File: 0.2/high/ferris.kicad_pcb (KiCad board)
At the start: 2 copper layers, 219.1 x 95.2 mm, 109 parts, among them J1 TYPE-C-31-M-12, K0_0 KEYSW, K0_1 KEYSW, K0_2 KEYSW, K0_3 KEYSW, K0_4 KEYSW, K0_5 KEYSW, K0_6 KEYSW, K0_7 KEYSW, K0_8 KEYSW, K0_9 KEYSW, K1_0 KEYSW, K1_1 KEYSW, K1_2 KEYSW, K1_3 KEYSW, K1_4 KEYSW, K1_5 KEYSW, K1_6 KEYSW, K1_7 KEYSW, K1_8 KEYSW, K1_9 KEYSW, K2_0 KEYSW, K2_1 KEYSW, K2_2 KEYSW, K2_3 KEYSW, K2_4 KEYSW, K2_5 KEYSW, K2_6 KEYSW, K2_7 KEYSW, K2_8 KEYSW, K2_9 KEYSW, K3_3 KEYSW, K3_4 KEYSW, K3_5 KEYSW, K3_6 KEYSW, Q1 PDTC123JT,215, SW1 B3U-1000P, U1 STM32F072CBT6, U2 MCP23017-E/SO, U3 MCP1700T-3302E/TT, U4 SRV05-4

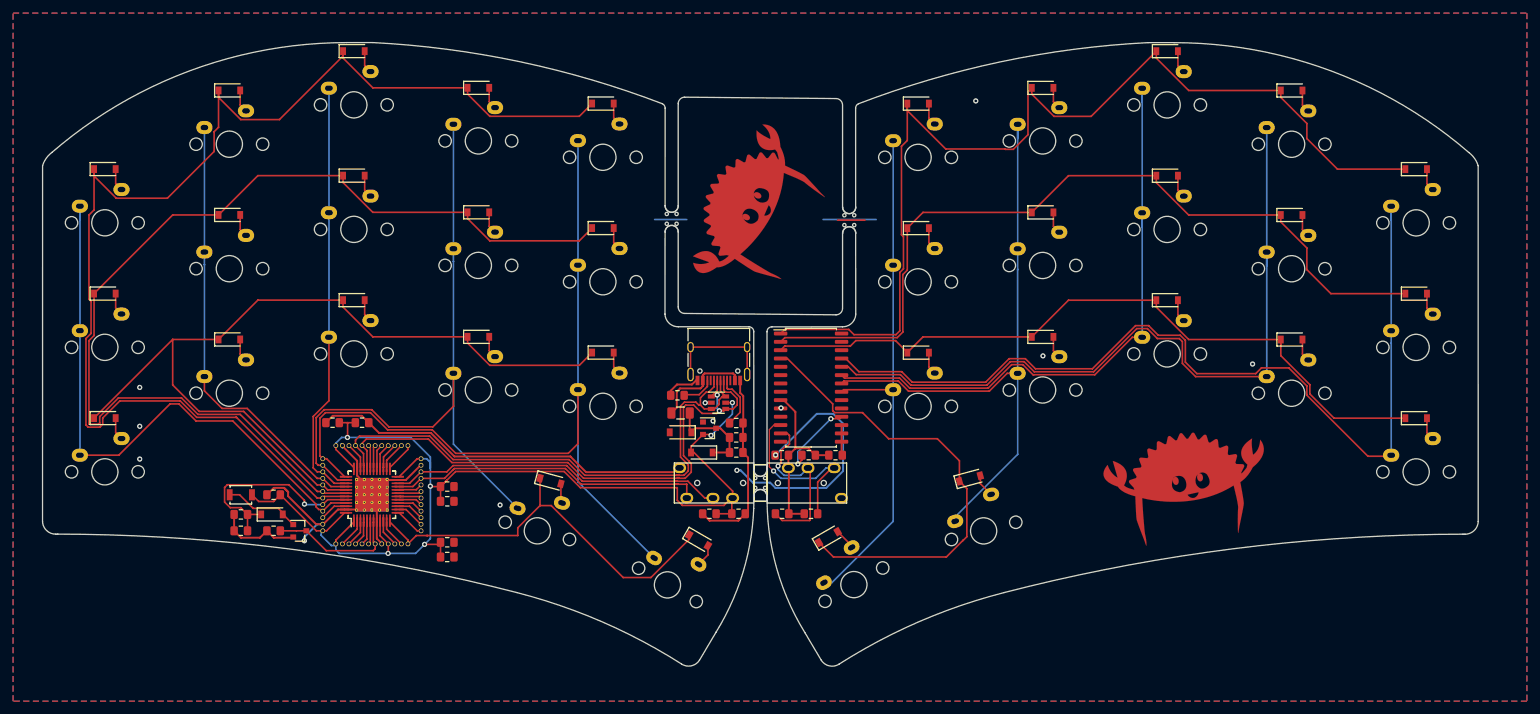
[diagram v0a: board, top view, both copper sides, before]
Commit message: Fix DRC violations down to 163
Mainly hole clearances, would need to fix the 5mm breakaway tab and perhaps solder mask clearances
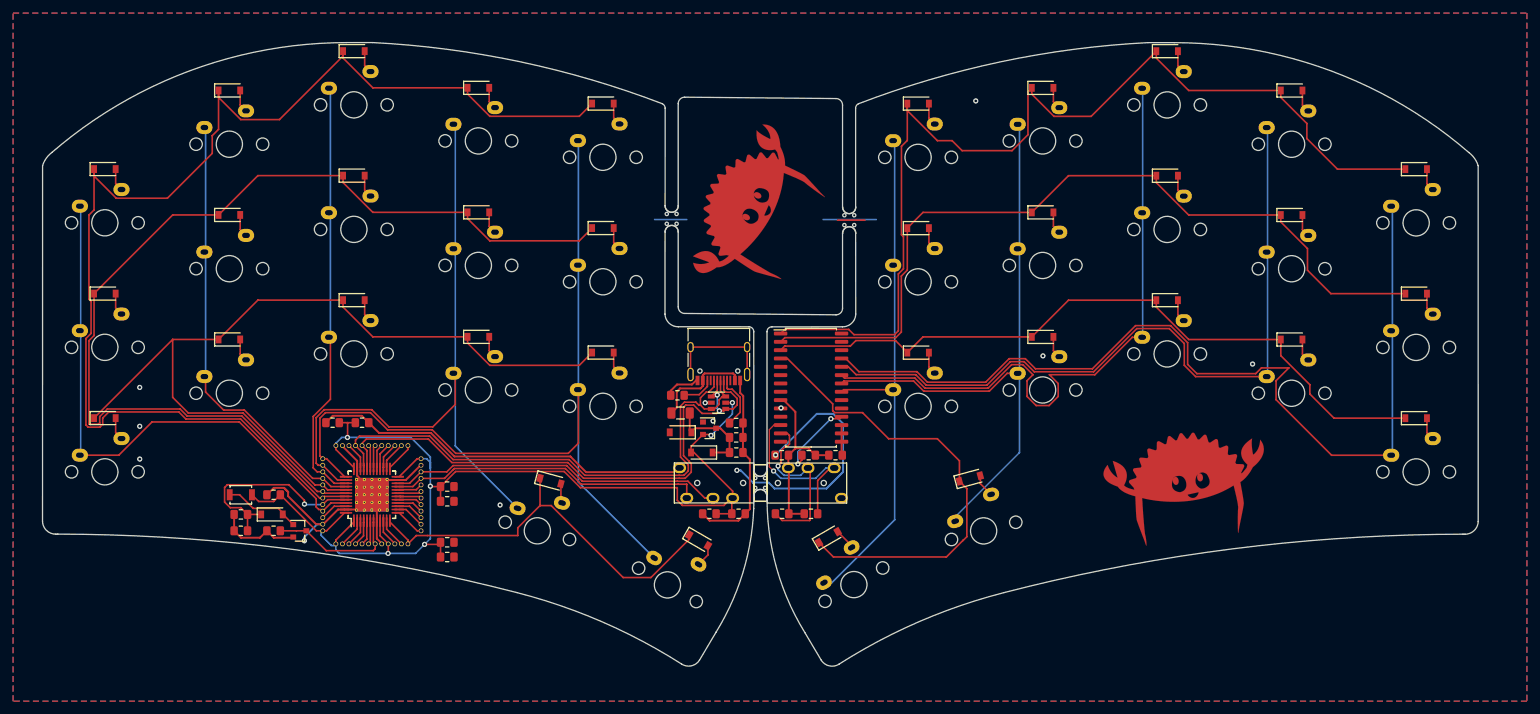
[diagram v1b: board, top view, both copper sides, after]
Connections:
- J1 pad A8: Net-(J1-PadA8) -> unconnected-(J1-SBU1-PadA8)
- J1 pad B8: Net-(J1-PadB8) -> unconnected-(J1-SBU2-PadB8)
- J1 pad S1: Net-(J1-PadS1) -> unconnected-(J1-SHIELD-PadS1)
- U1 pad 10: Net-(U1-Pad10) -> unconnected-(U1-PA0-Pad10)
- U1 pad 11: Net-(U1-Pad11) -> unconnected-(U1-PA1-Pad11)
- U1 pad 13: Net-(U1-Pad13) -> unconnected-(U1-PA3-Pad13)
- U1 pad 14: Net-(U1-Pad14) -> unconnected-(U1-PA4-Pad14)
- U1 pad 15: Net-(U1-Pad15) -> unconnected-(U1-PA5-Pad15)
- U1 pad 16: Net-(U1-Pad16) -> unconnected-(U1-PA6-Pad16)
- U1 pad 17: Net-(U1-Pad17) -> unconnected-(U1-PA7-Pad17)
- U1 pad 18: Net-(U1-Pad18) -> unconnected-(U1-PB0-Pad18)
- U1 pad 19: Net-(U1-Pad19) -> unconnected-(U1-PB1-Pad19)
- U1 pad 2: Net-(U1-Pad2) -> unconnected-(U1-PC13-Pad2)
- U1 pad 20: Net-(U1-Pad20) -> unconnected-(U1-PB2-Pad20)
- U1 pad 25: Net-(U1-Pad25) -> unconnected-(U1-PB12-Pad25)
- U1 pad 26: Net-(U1-Pad26) -> unconnected-(U1-PB13-Pad26)
- U1 pad 27: Net-(U1-Pad27) -> unconnected-(U1-PB14-Pad27)
- U1 pad 28: Net-(U1-Pad28) -> unconnected-(U1-PB15-Pad28)
- U1 pad 29: Net-(U1-Pad29) -> unconnected-(U1-PA8-Pad29)
- U1 pad 3: Net-(U1-Pad3) -> unconnected-(U1-PC14-Pad3)
- U1 pad 30: Net-(U1-Pad30) -> unconnected-(U1-PA9-Pad30)
- U1 pad 31: Net-(U1-Pad31) -> unconnected-(U1-PA10-Pad31)
- U1 pad 34: Net-(U1-Pad34) -> unconnected-(U1-PA13-Pad34)
- U1 pad 4: Net-(U1-Pad4) -> unconnected-(U1-PC15-Pad4)
- U1 pad 46: Net-(U1-Pad46) -> unconnected-(U1-PB9-Pad46)
- U1 pad 5: Net-(U1-Pad5) -> unconnected-(U1-PF0-Pad5)
- U1 pad 6: Net-(U1-Pad6) -> unconnected-(U1-PF1-Pad6)
- U2 pad 11: Net-(U2-Pad11) -> unconnected-(U2-NC-Pad11)
- U2 pad 14: Net-(U2-Pad14) -> unconnected-(U2-NC-Pad14)
- U2 pad 19: Net-(U2-Pad19) -> unconnected-(U2-INTB-Pad19)
- U2 pad 20: Net-(U2-Pad20) -> unconnected-(U2-INTA-Pad20)
- U2 pad 26: Net-(U2-Pad26) -> unconnected-(U2-GPA5-Pad26)
- U2 pad 27: Net-(U2-Pad27) -> unconnected-(U2-GPA6-Pad27)
- U2 pad 28: Net-(U2-Pad28) -> unconnected-(U2-GPA7-Pad28)
- U2 pad 5: Net-(U2-Pad5) -> unconnected-(U2-GPB4-Pad5)
- U2 pad 6: Net-(U2-Pad6) -> unconnected-(U2-GPB5-Pad6)
- U2 pad 7: Net-(U2-Pad7) -> unconnected-(U2-GPB6-Pad7)
- U2 pad 8: Net-(U2-Pad8) -> unconnected-(U2-GPB7-Pad8)
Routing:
- net unconnected-(J1-SHIELD-PadS1): track 0.00 -> 17.0 mm
- net Net-(J1-PadS1): track 17.0 -> 0.00 mm
- net /col7: track 93.5 -> 100.3 mm
- net unconnected-(U1-PA0-Pad10): track 0.00 -> 4.79 mm
- net Net-(U1-Pad10): track 4.79 -> 0.00 mm
- net unconnected-(U1-PB12-Pad25): track 0.00 -> 4.48 mm
- net unconnected-(U1-PA3-Pad13): track 0.00 -> 4.48 mm
- net Net-(U1-Pad25): track 4.48 -> 0.00 mm
- net Net-(U1-Pad13): track 4.48 -> 0.00 mm
- net unconnected-(U1-PC13-Pad2): track 0.00 -> 4.27 mm
- net unconnected-(U1-PB13-Pad26): track 0.00 -> 4.27 mm
- net unconnected-(U1-PA4-Pad14): track 0.00 -> 4.27 mm
- net unconnected-(U1-PA1-Pad11): track 0.00 -> 4.27 mm
- net Net-(U1-Pad26): track 4.27 -> 0.00 mm
- net Net-(U1-Pad2): track 4.27 -> 0.00 mm
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
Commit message: Fix more violations, down to 128
Mainly updated footprints where needed, kbd library is still not loaded, and various are missing from Resistor/Capacitor_SMD?
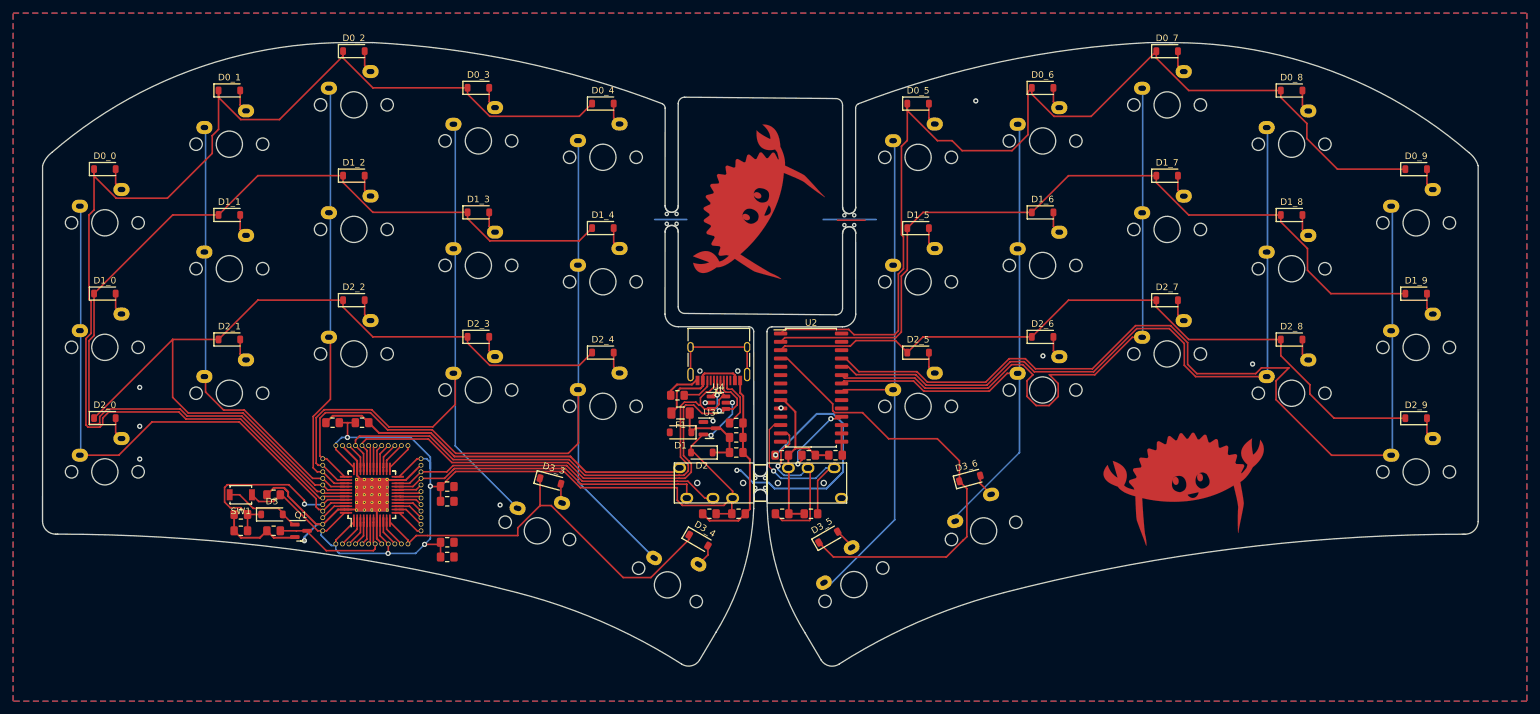
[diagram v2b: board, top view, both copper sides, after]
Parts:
- moved Q1 0.18 mm to (53.9, 89.0)
